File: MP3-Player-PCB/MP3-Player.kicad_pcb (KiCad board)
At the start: 4 copper layers, 110 parts, among them J101 Conn_ARM_SWD_TagConnect_TC2030, J201 Conn_01x02_Socket, J202 USB_C_Receptacle_USB2.0_16P, J301 Micro_SD_Card_Det1, Q301 AO3401A, Q302 2N7002H, SW301 1-1825910-4, SW302 1-1825910-4, SW303 1-1825910-4, SW304 1-1825910-4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

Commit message: Near completion of layout
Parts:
- J201, J202, J301, U402: moved to B.Cu
- moved U403 130.1 mm to (272.8, 36.8)
- moved C107 130.1 mm to (264.3, 48.5)
- moved C108 130.1 mm to (264.3, 51.0)
- moved C109 130.1 mm to (264.3, 53.6)
- moved C110 130.1 mm to (264.3, 56.1)
- moved C111 130.1 mm to (264.3, 58.6)
- moved C112 130.1 mm to (268.3, 48.5)
- moved C201 130.1 mm to (248.6, 32.7)
- moved C202 130.1 mm to (248.6, 35.2)
- moved C203 130.1 mm to (230.3, 21.0)
- moved C204 130.1 mm to (248.6, 37.7)
- moved C205 130.1 mm to (230.3, 24.0)
- moved C206 130.1 mm to (230.3, 27.0)
- moved C207 130.1 mm to (230.3, 30.0)
- moved C208 130.1 mm to (230.3, 33.0)
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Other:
- board outline added: 50 x 50.5 mm

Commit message: Finished rough layout. New Audio jack still required
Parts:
- R207, TH201, TP201: moved to B.Cu
- moved U403 185.0 mm to (106.2, 117.2)
- moved R104 177.2 mm to (123.6, 142.4), turned to -90 degrees
- moved D102 177.1 mm to (123.6, 144.4), turned to 90 degrees
- moved R103 176.5 mm to (125.6, 142.4), turned to -90 degrees
- moved R403 176.5 mm to (112.2, 123.6)
- moved D101 176.4 mm to (125.6, 144.4), turned to 90 degrees
- moved R404 176.0 mm to (112.2, 125.2)
- moved C405 175.8 mm to (111.9, 116.4), turned to 135 degrees
- moved R405 175.5 mm to (112.2, 126.8)
- moved C109 175.3 mm to (111.2, 138.8), turned to 135 degrees
- moved R406 174.3 mm to (118.3, 107.8), turned to 180 degrees
- moved R101 174.0 mm to (121.8, 128.4), turned to -45 degrees
- moved R402 169.6 mm to (113.9, 110.2), turned to 90 degrees
- moved FB201 169.4 mm to (106.0, 128.0)
- moved R401 168.6 mm to (116.5, 110.2), turned to 90 degrees
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
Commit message: Final Layout
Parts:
- moved J201 44.7 mm to (103.0, 129.4), turned to 0 degrees
- moved U402 44.6 mm to (104.1, 119.3), turned to -90 degrees
- moved C216 6.95 mm to (139.8, 131.2), turned to 180 degrees
- moved C214 4.96 mm to (107.4, 126.8)
- moved C215 4.96 mm to (113.8, 126.8)
- moved U203 4.96 mm to (110.6, 126.8)
- moved FB201 4.32 mm to (110.0, 129.6)
- moved C212 4.32 mm to (109.0, 132.2)
- moved C213 4.32 mm to (111.0, 132.2)
- moved C217 3.46 mm to (139.8, 124.8), turned to 180 degrees
- moved R403 3.39 mm to (109.8, 121.2)
- moved R404 3.39 mm to (109.8, 122.8)
- moved R405 3.39 mm to (109.8, 124.4)
- moved U204 3.01 mm to (139.8, 128.0), turned to 90 degrees
- moved U403 2.03 mm to (104.2, 117.8)

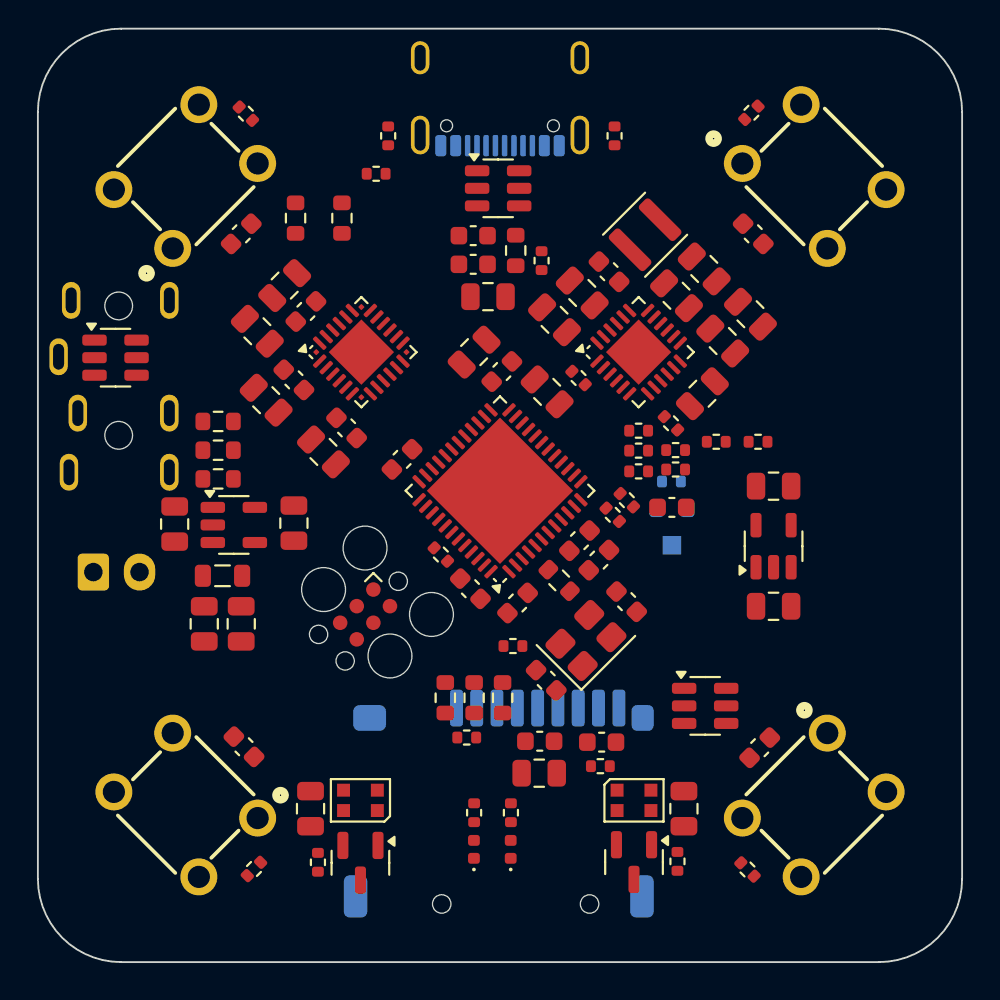
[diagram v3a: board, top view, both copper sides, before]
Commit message: Adding GND vias
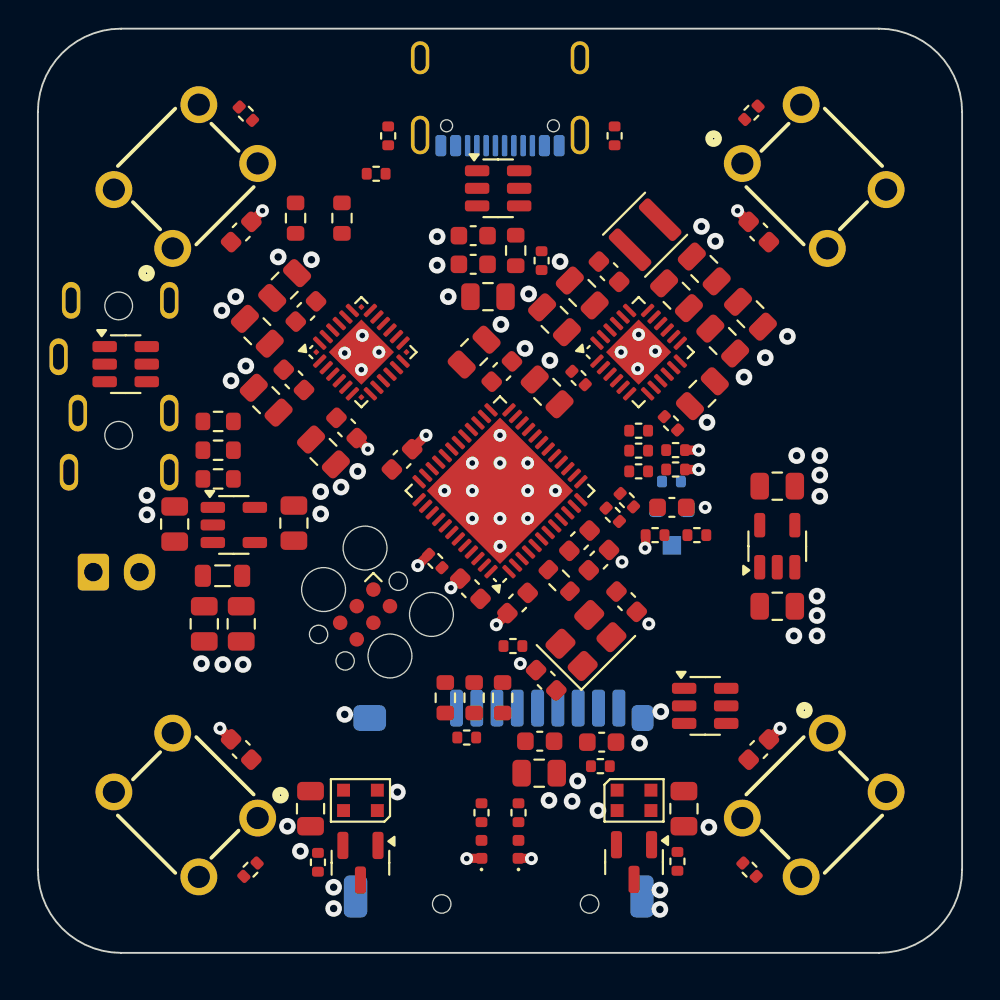
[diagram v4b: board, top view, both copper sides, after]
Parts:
- moved R214 6.04 mm to (135.7, 127.4)
- moved R216 6.04 mm to (133.4, 127.4)
- moved U403 0.65 mm to (104.8, 118.2)
- moved R101 0.46 mm to (121.5, 128.8)
- moved D101 0.42 mm to (126.0, 144.4)
- moved D102 0.41 mm to (124.0, 144.4)
- moved R103 0.41 mm to (126.0, 142.4)
- moved R104 0.40 mm to (124.0, 142.4)
- moved C110 0.32 mm to (139.0, 111.0), turned to 135 degrees
- moved C109 0.21 mm to (111.0, 139.0)
- moved C216 0.20 mm to (140.0, 131.2), turned to 0 degrees
- moved C217 0.20 mm to (140.0, 124.8), turned to 0 degrees
- moved U204 0.20 mm to (140.0, 128.0)
- moved R304 0.19 mm to (111.5, 145.5)
- moved C108 0.11 mm to (139.0, 139.0)
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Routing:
- net GND: track 0.00 -> 11.5 mm, vias 0 -> 90
- added copper zone on In1.Cu, net GND
- added copper zone on In2.Cu, net GND
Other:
- board size 50 x 50.5 mm -> 50 x 50 mm

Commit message: Much better initial layout
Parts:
- removed R403, R404, R405: 0R, Resistor_SMD:R_0603_1608Metric
- C101, C115, C203, C209, C211, C212, C213, C301, C304, C305, C401, C404, C405, C406: footprint Capacitor_SMD:C_0805_2012Metric -> Capacitor_SMD:C_0603_1608Metric
- C102, C103, C104, C105, C106, C107, C108, C109, C110, C111, C112, C201, C202, C204, C302, C303, C402, C403, C407: footprint Capacitor_SMD:C_0603_1608Metric -> Capacitor_SMD:C_0402_1005Metric
- moved U402 41.6 mm to (145.7, 120.3)
- moved U403 41.3 mm to (146.0, 119.1)
- moved J201 41.3 mm to (144.2, 129.3)
- moved C216 31.7 mm to (109.1, 124.0), turned to 180 degrees
- moved C217 31.4 mm to (109.1, 130.6), turned to 180 degrees
- moved U204 30.9 mm to (109.1, 127.3), turned to -90 degrees
- moved R304 28.9 mm to (131.8, 124.9), turned to 135 degrees
- moved FB201 27.9 mm to (137.7, 126.9)
- moved C214 27.9 mm to (135.2, 124.1)
- moved C215 27.9 mm to (141.6, 124.0)
- moved U203 27.9 mm to (138.3, 124.1)
- moved C212 27.9 mm to (136.8, 129.5)
- moved C213 27.9 mm to (138.8, 129.5)
- moved C109 24.0 mm to (131.0, 125.7), turned to -45 degrees
- moved R308 23.5 mm to (121.0, 120.0), turned to -45 degrees
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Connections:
- U401 pad 2: /DAC/DAC_BCLK_PIN -> DAC_BCLK
- U401 pad 3: /DAC/DAC_FSYNC_PIN -> DAC_FSYNC
- U401 pad 5: /DAC/DAC_DIN_PIN -> DAC_DIN
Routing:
- net GND: track 11.5 -> 0.00 mm, vias 90 -> 20

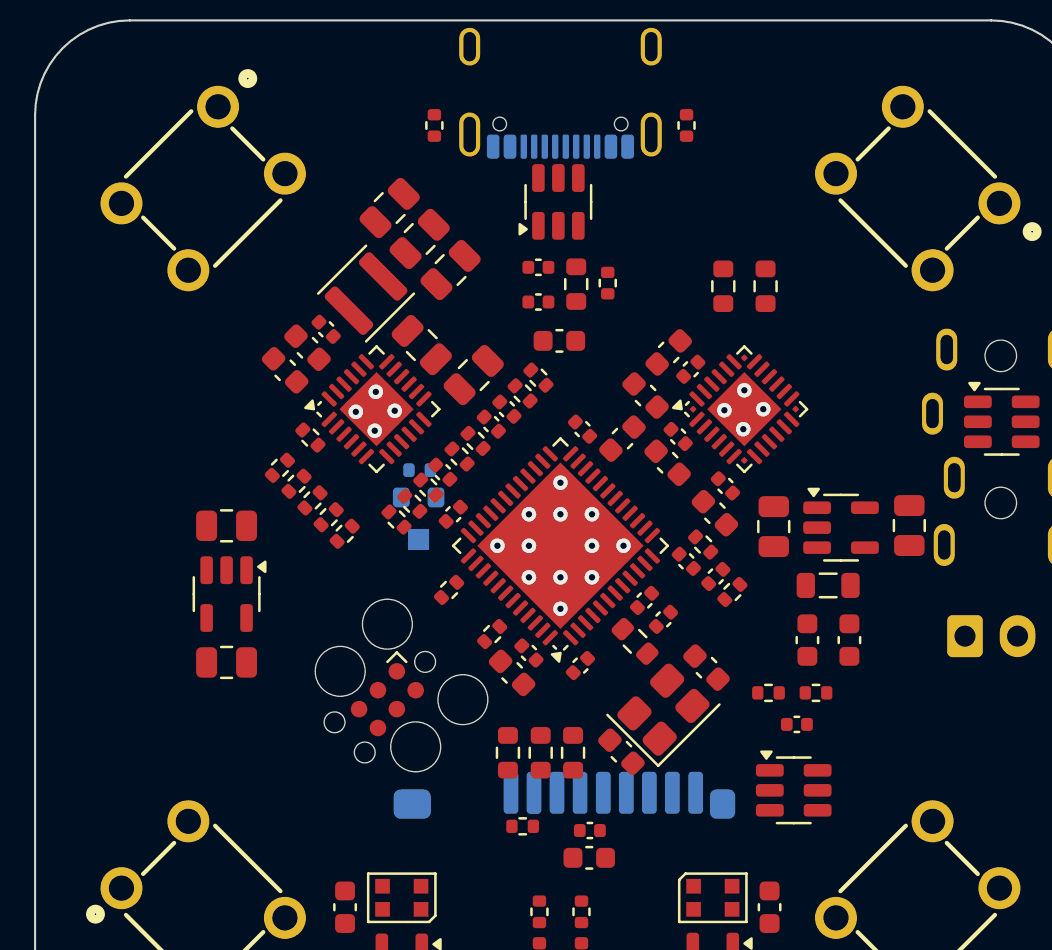
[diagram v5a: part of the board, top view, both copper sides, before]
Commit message: Cleaned up layout yet again for proper routing. Started preliminary routing
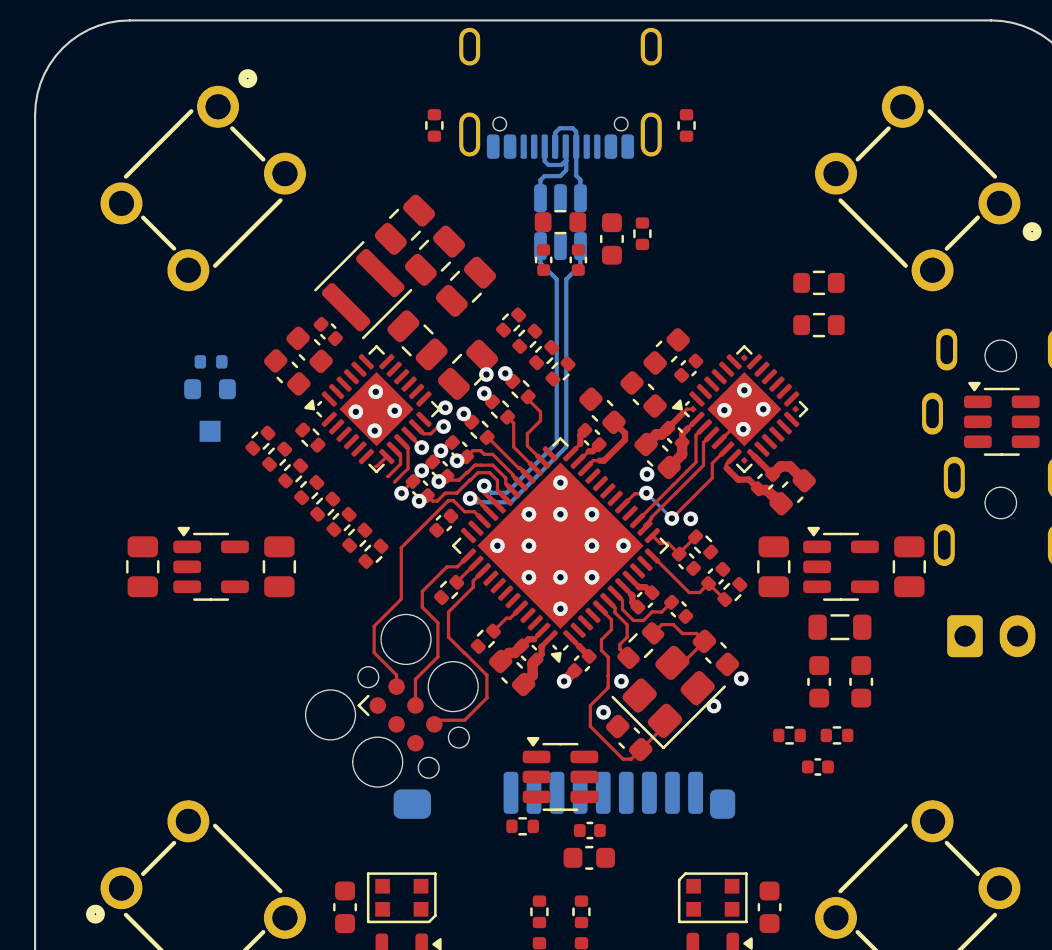
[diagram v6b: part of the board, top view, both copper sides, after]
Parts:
- R305, R306, R307: footprint Resistor_SMD:R_0603_1608Metric -> Resistor_SMD:R_0402_1005Metric
- U202: moved to B.Cu
- moved R306 17.3 mm to (123.1, 117.5), turned to 135 degrees
- moved R307 16.7 mm to (122.1, 118.5), turned to 135 degrees
- moved R305 15.4 mm to (121.1, 119.5), turned to 135 degrees
- moved R207 11.2 mm to (108.4, 116.2)
- moved TH201 11.2 mm to (108.3, 117.5)
- moved TP201 11.2 mm to (108.3, 119.5)
- moved U301 11.1 mm to (125.0, 136.0)
- moved R309 6.83 mm to (122.7, 114.4), turned to -135 degrees
- moved C203 5.46 mm to (127.5, 110.4), turned to -90 degrees
- moved R308 5.45 mm to (123.4, 115.2), turned to -135 degrees
- moved C217 5.20 mm to (111.6, 126.0), turned to -90 degrees
- moved R402 4.55 mm to (137.3, 112.5), turned to 0 degrees
- moved C216 4.44 mm to (105.1, 126.0), turned to -90 degrees
- moved R208 4.09 mm to (116.1, 125.4), turned to -135 degrees
- moved C404 3.83 mm to (136.1, 122.5), turned to 45 degrees
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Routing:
- net USB_MCU_D+: track 0.00 -> 17.1 mm, vias 0 -> 1
- net GND: track 0.00 -> 15.9 mm, vias 20 -> 32
- net USB_MCU_D-: track 0.00 -> 15.5 mm, vias 0 -> 1
- net /MCU/SWD_SWDIO: track 0.00 -> 12.8 mm
- net /MCU/HSE_IN: track 0.00 -> 11.6 mm
- net /MCU/SWD_SWO: track 0.00 -> 10.5 mm
- net +3.3V: track 0.00 -> 10.2 mm
- net /MCU/SWD_SWCLK: track 0.00 -> 9.07 mm
- net DAC_DIN: track 0.00 -> 7.49 mm, vias 0 -> 2
- net DAC_BCLK: track 0.00 -> 5.79 mm
- net DAC_FSYNC: track 0.00 -> 5.79 mm
- net BUTTON_4: track 0.00 -> 5.68 mm, vias 0 -> 1
- net /Power/USB_CON_D-: track 0.00 -> 5.36 mm
- net /MCU/HSE_OUT_RES: track 0.00 -> 5.24 mm
- net /Power/USB_CON_D+: track 0.00 -> 5.06 mm
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
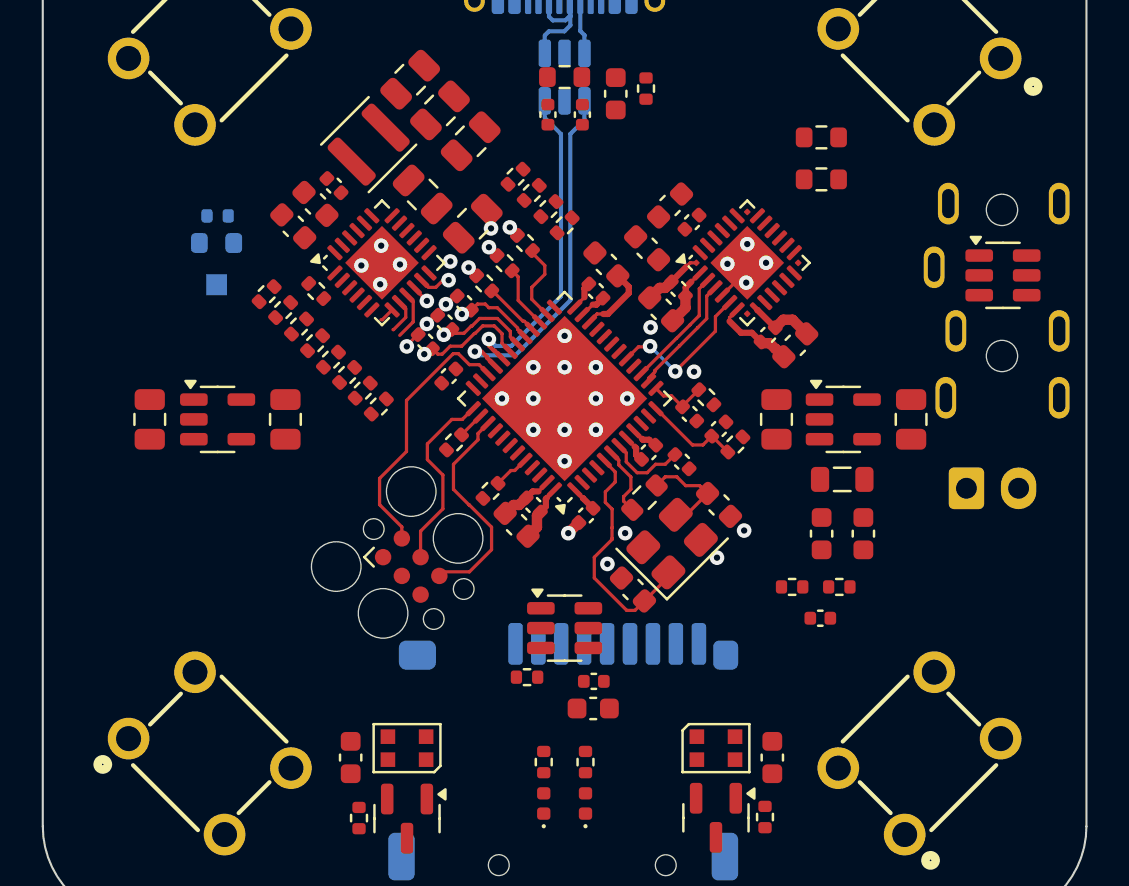
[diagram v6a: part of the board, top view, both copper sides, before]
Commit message: Routing more mcu signals
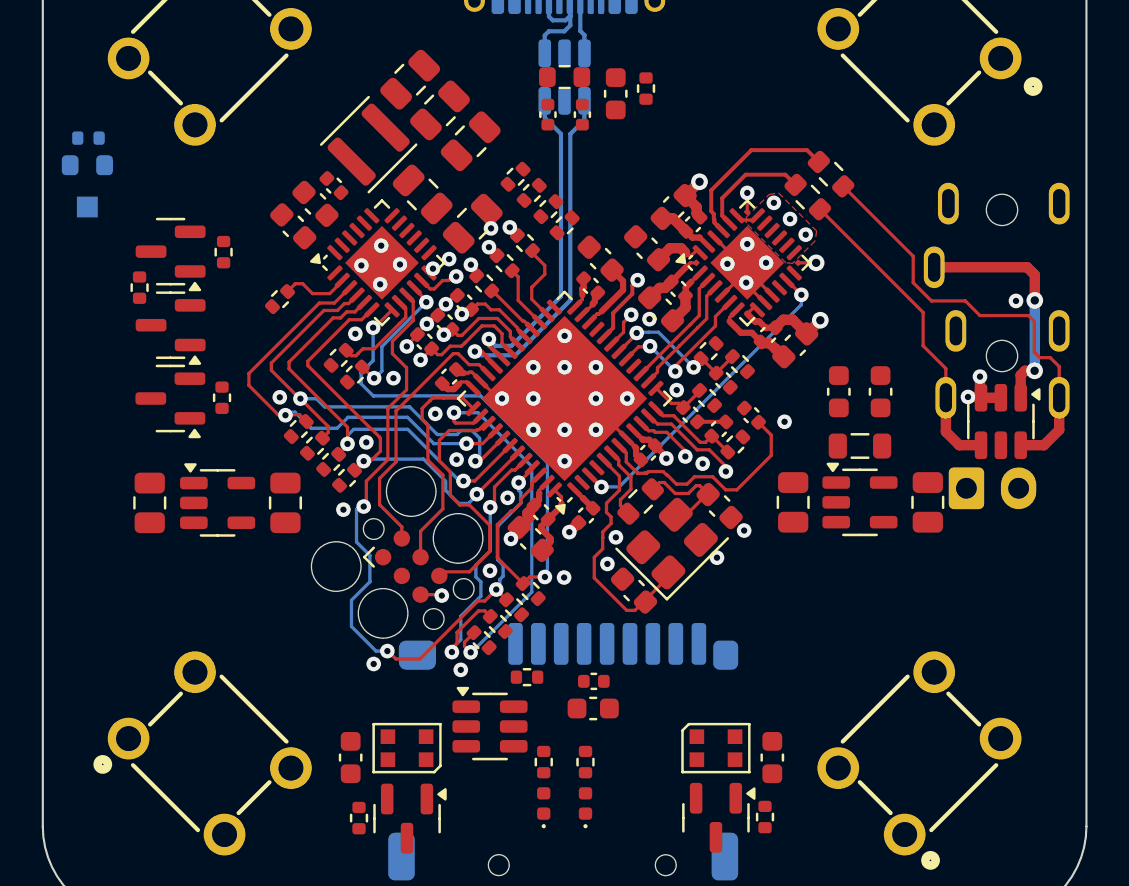
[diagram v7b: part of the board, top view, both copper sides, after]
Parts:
- added Q303: AO3401A, Package_TO_SOT_SMD:SOT-23, F.Cu at (106.1, 125.0)
- added Q304: AO3401A, Package_TO_SOT_SMD:SOT-23, F.Cu at (106.1, 121.5)
- added Q305: 2N7002H, Package_TO_SOT_SMD:SOT-23, F.Cu at (106.1, 118.0)
- added R313: 220k, Resistor_SMD:R_0402_1005Metric, F.Cu at (108.6, 125.0)
- added R314: 220k, Resistor_SMD:R_0402_1005Metric, F.Cu at (108.7, 118.0)
- added R315: 56k, Resistor_SMD:R_0402_1005Metric, F.Cu at (104.6, 119.7)
- R309: value 56k -> 220k
- moved R213 14.6 mm to (123.4, 134.2), turned to 135 degrees
- moved R215 12.7 mm to (122.6, 135.0), turned to -45 degrees
- moved C112 12.3 mm to (132.6, 124.1), turned to -45 degrees
- moved R214 12.0 mm to (131.9, 122.7), turned to -135 degrees
- moved R216 11.7 mm to (133.4, 123.3), turned to -45 degrees
- moved R406 9.57 mm to (121.0, 136.6), turned to 135 degrees
- moved C212 7.36 mm to (140.1, 124.7), turned to 90 degrees
- moved TH201 7.22 mm to (102.1, 113.8)
- moved TP201 7.22 mm to (102.1, 115.8)
- moved R207 7.22 mm to (102.2, 112.5)
- moved U403 7.00 mm to (145.9, 126.1), turned to -90 degrees
- moved C213 6.90 mm to (138.1, 124.7), turned to 90 degrees
- moved R210 6.68 mm to (113.0, 127.3)
- moved R212 6.67 mm to (113.8, 128.0)
- moved R209 6.64 mm to (112.3, 126.5)
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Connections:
- net Net-(D101-A) renamed /MCU/BAT_STATUS_LED_RES
- net Net-(D102-A) renamed /MCU/BAT_CHARGING_LED_RES
- net Net-(Q301-G) renamed /Peripherals/LED_GATE
- C210 pad 1: /Power/BAT_BAT -> +VBAT
- J201 pad 1: /Power/BAT_BAT -> +VBAT
- R309 pad 1: +3.3V -> +VBAT
- R309 pad 2: BUTTON_4 -> /Peripherals/BUTTON4_GATE
- SW304 pad 1: BUTTON_4 -> /Peripherals/BUTTON4_GATE
- SW304 pad 2: BUTTON_4 -> /Peripherals/BUTTON4_GATE
- U101 pad 16: DAC_GPO -> unconnected-(U101-PA6-Pad16)
- U101 pad 3: unconnected-(U101-PC14-Pad3) -> DAC_GPO
- U201 pad 12: unconnected-(U201-QON-Pad12) -> BAT_QON
- U201 pad 13: /Power/BAT_BAT -> +VBAT
- U201 pad 14: /Power/BAT_BAT -> +VBAT
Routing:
- net BAT_NCE: track 2.32 -> 35.0 mm, vias 0 -> 4
- net AUDIO_JACK_DET: track 1.29 -> 29.5 mm, vias 0 -> 4
- net BAT_INT: track 0.73 -> 28.0 mm, vias 0 -> 2
- net GND: track 15.9 -> 41.7 mm, vias 32 -> 58
- net BAT_STAT: track 0.00 -> 22.8 mm, vias 0 -> 2
- net BAT_NPG: track 0.00 -> 22.0 mm, vias 0 -> 2
- net BAT_SDA: track 0.00 -> 21.1 mm, vias 0 -> 2
- net /DAC/DAC_AUDIO_RIGHT: track 0.00 -> 20.7 mm
- net BAT_SCL: track 0.00 -> 20.6 mm, vias 0 -> 2
- net DAC_GPO: track 0.00 -> 15.5 mm, vias 0 -> 2
- net /DAC/DAC_AUDIO_LEFT: track 0.00 -> 15.1 mm
- net /MCU/BOOT: track 1.77 -> 14.1 mm, vias 0 -> 2
- net /DAC/DAC_PIN_R: track 0.00 -> 8.34 mm
- net /MCU/NRST: track 3.83 -> 11.3 mm
- net BAT_CHARGE: track 0.00 -> 7.37 mm, vias 0 -> 2
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- added copper zone on F.Cu, net GND

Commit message: Continuing routing
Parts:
- moved R309 13.1 mm to (110.5, 119.4)
- moved R302 3.58 mm to (122.0, 118.7), turned to -45 degrees
- moved R310 3.31 mm to (122.1, 113.4)
- moved R308 1.12 mm to (122.9, 114.1)
- moved R307 0.99 mm to (122.8, 117.8)
- moved R306 0.81 mm to (123.7, 117.0)
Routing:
- net /Peripherals/SD_CARD_MISO_PIN: track 0.57 -> 28.7 mm, vias 1 -> 2
- net /Peripherals/SD_CARD_SCK_PIN: track 0.54 -> 25.7 mm
- net /Peripherals/SD_CARD_MOSI_PIN: track 0.65 -> 24.0 mm
- net BUTTON_4: track 5.99 -> 20.0 mm, vias 1 -> 2
- net SD_CARD_MOSI: track 2.71 -> 3.91 mm
- net SD_CARD_MISO: track 3.00 -> 4.08 mm
- net SD_CARD_SCK: track 3.64 -> 4.65 mm
- net /Power/BAT_ILIM: track 6.41 -> 7.04 mm
- net BAT_INT: track 28.0 -> 28.5 mm
- net GND: track 41.7 -> 41.5 mm, vias 58 -> 61
